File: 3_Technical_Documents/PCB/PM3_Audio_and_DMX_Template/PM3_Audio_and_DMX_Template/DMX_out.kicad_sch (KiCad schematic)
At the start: 16 parts, among them U1 6N136S, U2 CRE1S0505SC, U3 ST485E

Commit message: new push
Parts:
- renumbered C3 to C11, C4 to C12, C5 to C13, R4 to R10, R5 to R11, R6 to R12, R7 to R13, R2 to R8, R3 to R9, U1 to U3, U2 to U4, U3 to U5
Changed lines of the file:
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@@
 		(dnp no)
 		(fields_autoplaced yes)
-		(property "Reference" "R6"
+		(property "Reference" "R12"
 			(at 243.84 55.8799 0)
 			(effects
@@
 			(project "HW_template"
 				(path "/1f276d59-ad9b-4e70-a842-f3b7e562eb9b/284106b9-cc72-4299-bd54-f70997210d49"
-					(reference "R6")
+					(reference "R12")
 					(unit 1)
 				)
@@
 		(dnp no)
 		(fields_autoplaced yes)
-		(property "Reference" "U2"
+		(property "Reference" "U4"
 			(at 106.68 113.03 0)
 			(effects
@@
 			(project "HW_template"
 				(path "/1f276d59-ad9b-4e70-a842-f3b7e562eb9b/284106b9-cc72-4299-bd54-f70997210d49"
-					(reference "U2")
+					(reference "U4")
 					(unit 1)
 				)
@@
 		(dnp no)
 		(fields_autoplaced yes)
-		(property "Reference" "R7"
+		(property "Reference" "R13"
 			(at 243.84 68.5799 0)
 			(effects
@@
 			(project "HW_template"
 				(path "/1f276d59-ad9b-4e70-a842-f3b7e562eb9b/284106b9-cc72-4299-bd54-f70997210d49"
-					(reference "R7")
+					(reference "R13")
 					(unit 1)
 				)
@@
 		(dnp no)
 		(fields_autoplaced yes)
-		(property "Reference" "R2"
+		(property "Reference" "R8"
 			(at 85.09 60.96 90)
 			(effects
@@
 			(project "HW_template"
 				(path "/1f276d59-ad9b-4e70-a842-f3b7e562eb9b/284106b9-cc72-4299-bd54-f70997210d49"
-					(reference "R2")
+					(reference "R8")
 					(unit 1)
 				)
@@
 		(on_board yes)
 		(dnp no)
-		(property "Reference" "R3"
+		(property "Reference" "R9"
 			(at 123.19 62.2299 0)
 			(effects
@@
 			(project "HW_template"
 				(path "/1f276d59-ad9b-4e70-a842-f3b7e562eb9b/284106b9-cc72-4299-bd54-f70997210d49"
-					(reference "R3")
+					(reference "R9")
 					(unit 1)
 				)
@@
 		(on_board yes)
 		(dnp no)
-		(property "Reference" "#PWR018"
+		(property "Reference" "#PWR033"
 			(at 88.9 62.23 0)
 			(effects
@@
 			(project "vuMeter_Lightorgan"
 				(path "/1f276d59-ad9b-4e70-a842-f3b7e562eb9b/284106b9-cc72-4299-bd54-f70997210d49"
-					(reference "#PWR018")
+					(reference "#PWR033")
 					(unit 1)
 				)
@@
 		(dnp no)
 		(fields_autoplaced yes)
-		(property "Reference" "R5"
+		(property "Reference" "R11"
 			(at 243.84 43.1799 0)
 			(effects
@@
 			(project "HW_template"
 				(path "/1f276d59-ad9b-4e70-a842-f3b7e562eb9b/284106b9-cc72-4299-bd54-f70997210d49"
-					(reference "R5")
+					(reference "R11")
 					(unit 1)
 				)
@@
 		(dnp no)
 		(fields_autoplaced yes)
-		(property "Reference" "C3"
+		(property "Reference" "C11"
 			(at 88.9 124.4599 0)
 			(effects
@@
 			(project "HW_template"
 				(path "/1f276d59-ad9b-4e70-a842-f3b7e562eb9b/284106b9-cc72-4299-bd54-f70997210d49"
-					(reference "C3")
+					(reference "C11")
 					(unit 1)
 				)
@@
 		(dnp no)
 		(fields_autoplaced yes)
-		(property "Reference" "C4"
+		(property "Reference" "C12"
 			(at 129.54 124.4599 0)
 			(effects
@@
 			(project "HW_template"
 				(path "/1f276d59-ad9b-4e70-a842-f3b7e562eb9b/284106b9-cc72-4299-bd54-f70997210d49"
-					(reference "C4")
+					(reference "C12")
 					(unit 1)
 				)
@@
 		(dnp no)
 		(fields_autoplaced yes)
-		(property "Reference" "U1"
+		(property "Reference" "U3"
 			(at 106.68 53.34 0)
 			(effects
@@
 			(project ""
 				(path "/1f276d59-ad9b-4e70-a842-f3b7e562eb9b/284106b9-cc72-4299-bd54-f70997210d49"
-					(reference "U1")
+					(reference "U3")
 					(unit 1)
 				)
@@
 		(dnp no)
 		(fields_autoplaced yes)
-		(property "Reference" "U3"
+		(property "Reference" "U5"
 			(at 179.9941 44.45 0)
 			(effects
@@
 			(project "HW_template"
 				(path "/1f276d59-ad9b-4e70-a842-f3b7e562eb9b/284106b9-cc72-4299-bd54-f70997210d49"
-					(reference "U3")
+					(reference "U5")
 					(unit 1)
 				)
@@
 		(dnp no)
 		(fields_autoplaced yes)
-		(property "Reference" "R4"
+		(property "Reference" "R10"
 			(at 140.97 124.4599 0)
 			(effects
@@
 			(project "HW_template"
 				(path "/1f276d59-ad9b-4e70-a842-f3b7e562eb9b/284106b9-cc72-4299-bd54-f70997210d49"
-					(reference "R4")
+					(reference "R10")
 					(unit 1)
 				)
@@
 		(dnp no)
 		(fields_autoplaced yes)
-		(property "Reference" "C5"
+		(property "Reference" "C13"
 			(at 194.31 71.1199 0)
 			(effects
@@
 			(project "HW_template"
 				(path "/1f276d59-ad9b-4e70-a842-f3b7e562eb9b/284106b9-cc72-4299-bd54-f70997210d49"
-					(reference "C5")
-					(unit 1)
-				)
+					(reference "C13")
+					(unit 1)
+				)

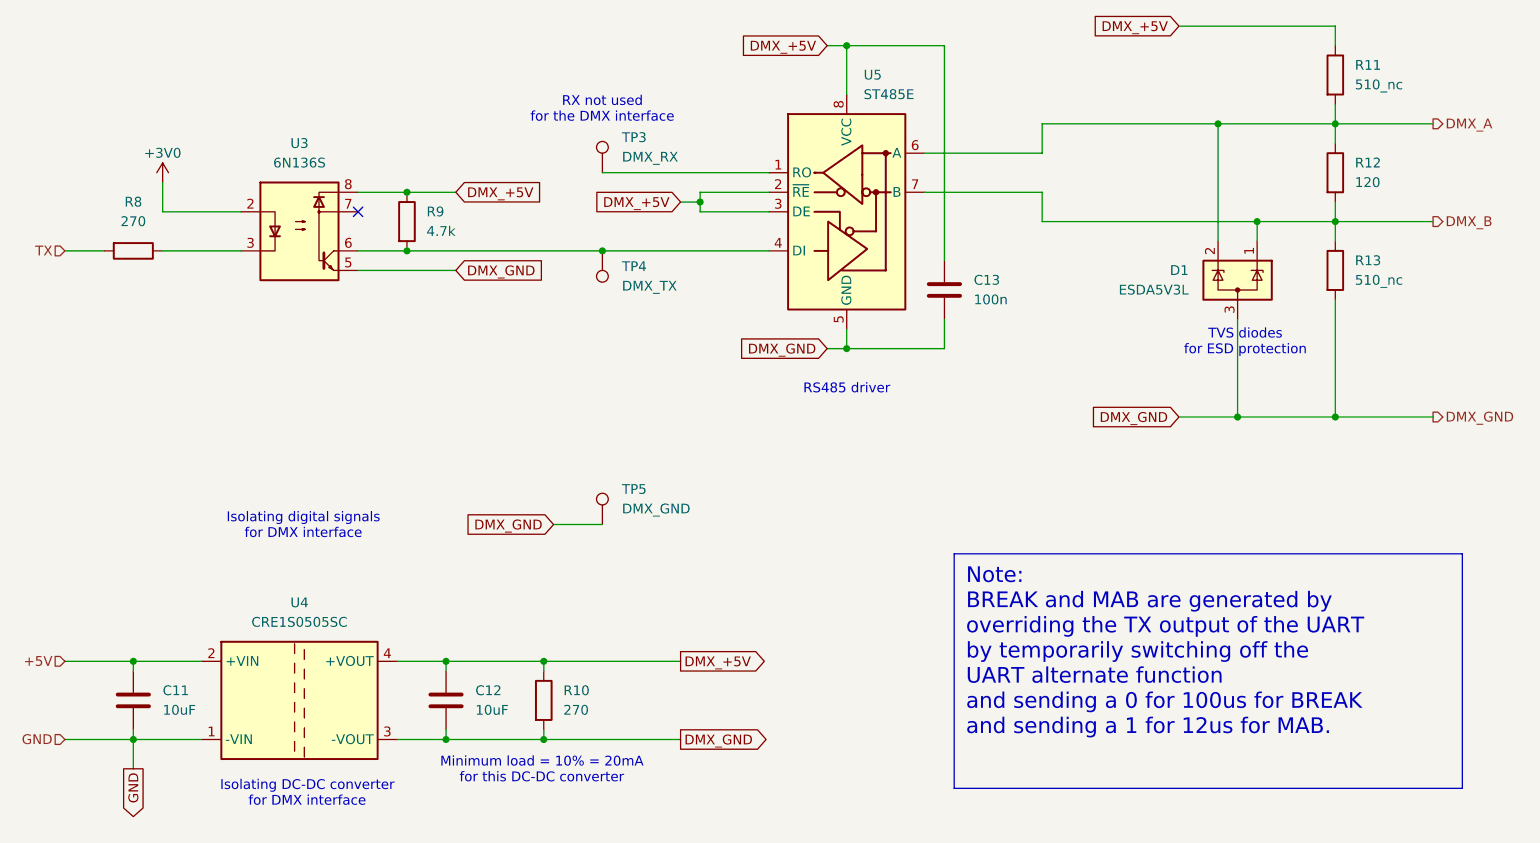
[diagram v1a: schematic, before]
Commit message: rework esp32, codec and layout
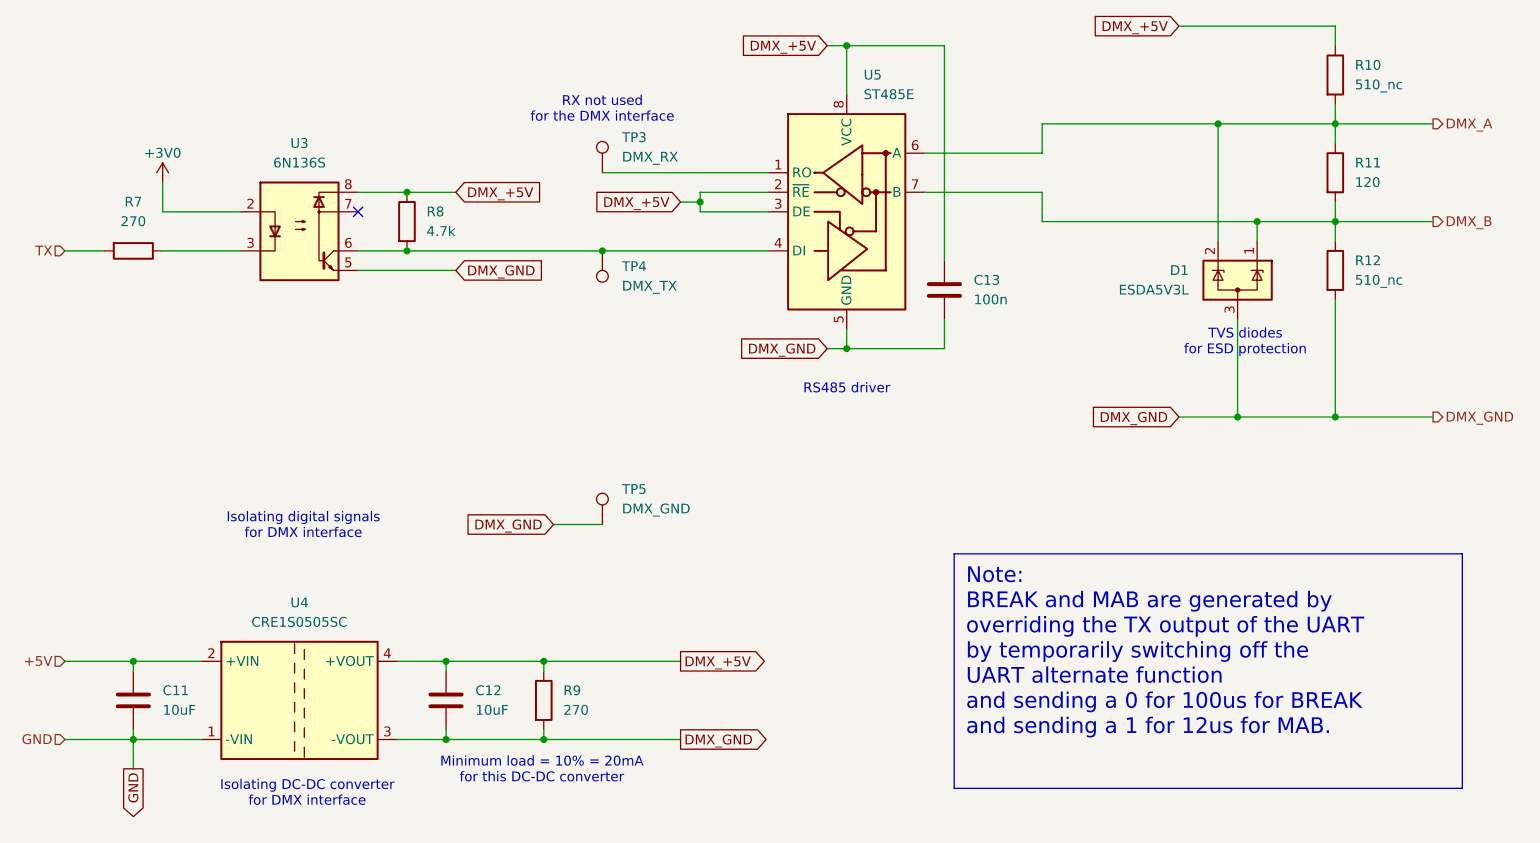
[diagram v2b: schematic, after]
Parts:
- renumbered R11 to R10, R12 to R11, R13 to R12, R8 to R7, R9 to R8, R10 to R9
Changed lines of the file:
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@@
 		(dnp no)
 		(fields_autoplaced yes)
-		(property "Reference" "R12"
+		(property "Reference" "R11"
 			(at 243.84 55.8799 0)
 			(effects
@@
 			(project "HW_template"
 				(path "/1f276d59-ad9b-4e70-a842-f3b7e562eb9b/284106b9-cc72-4299-bd54-f70997210d49"
-					(reference "R12")
+					(reference "R11")
 					(unit 1)
 				)
@@
 		(dnp no)
 		(fields_autoplaced yes)
-		(property "Reference" "R13"
+		(property "Reference" "R12"
 			(at 243.84 68.5799 0)
 			(effects
@@
 			(project "HW_template"
 				(path "/1f276d59-ad9b-4e70-a842-f3b7e562eb9b/284106b9-cc72-4299-bd54-f70997210d49"
-					(reference "R13")
+					(reference "R12")
 					(unit 1)
 				)
@@
 		(dnp no)
 		(fields_autoplaced yes)
-		(property "Reference" "R8"
+		(property "Reference" "R7"
 			(at 85.09 60.96 90)
 			(effects
@@
 			(project "HW_template"
 				(path "/1f276d59-ad9b-4e70-a842-f3b7e562eb9b/284106b9-cc72-4299-bd54-f70997210d49"
-					(reference "R8")
+					(reference "R7")
 					(unit 1)
 				)
@@
 		(on_board yes)
 		(dnp no)
-		(property "Reference" "R9"
+		(property "Reference" "R8"
 			(at 123.19 62.2299 0)
 			(effects
@@
 			(project "HW_template"
 				(path "/1f276d59-ad9b-4e70-a842-f3b7e562eb9b/284106b9-cc72-4299-bd54-f70997210d49"
-					(reference "R9")
+					(reference "R8")
 					(unit 1)
 				)
@@
 		(dnp no)
 		(fields_autoplaced yes)
-		(property "Reference" "R11"
+		(property "Reference" "R10"
 			(at 243.84 43.1799 0)
 			(effects
@@
 			(project "HW_template"
 				(path "/1f276d59-ad9b-4e70-a842-f3b7e562eb9b/284106b9-cc72-4299-bd54-f70997210d49"
-					(reference "R11")
+					(reference "R10")
 					(unit 1)
 				)
@@
 		(dnp no)
 		(fields_autoplaced yes)
-		(property "Reference" "R10"
+		(property "Reference" "R9"
 			(at 140.97 124.4599 0)
 			(effects
@@
 			(project "HW_template"
 				(path "/1f276d59-ad9b-4e70-a842-f3b7e562eb9b/284106b9-cc72-4299-bd54-f70997210d49"
-					(reference "R10")
-					(unit 1)
-				)
+					(reference "R9")
+					(unit 1)
+				)

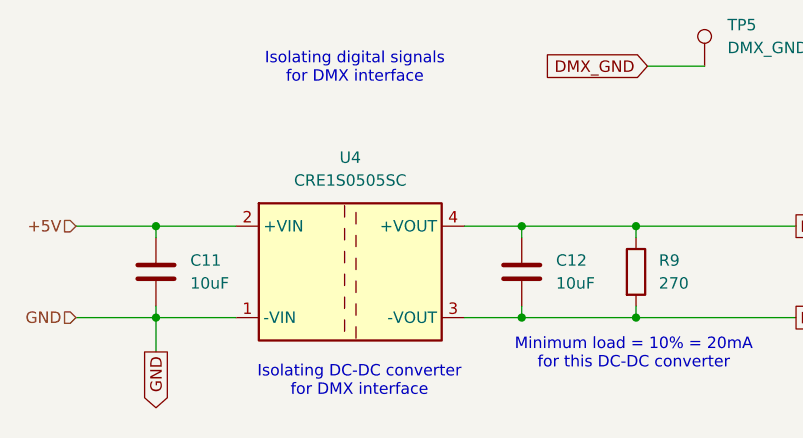
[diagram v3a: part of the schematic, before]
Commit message: schematics, layout and bom updated (to match corrections)
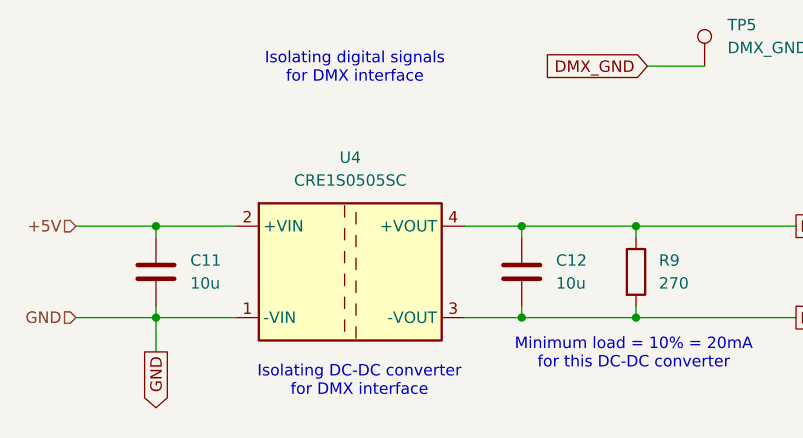
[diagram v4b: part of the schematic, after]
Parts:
- C11, C12: value 10uF -> 10u
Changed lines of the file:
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@@
 			)
 		)
-		(property "Value" "10uF"
+		(property "Value" "10u"
 			(at 88.9 126.9999 0)
 			(effects
@@
 			)
 		)
-		(property "Value" "10uF"
+		(property "Value" "10u"
 			(at 129.54 126.9999 0)
 			(effects
